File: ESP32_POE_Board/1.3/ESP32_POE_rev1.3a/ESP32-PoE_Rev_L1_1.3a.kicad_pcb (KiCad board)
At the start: 4 copper layers, 28 x 80 mm, 161 parts, among them J1 RS1-02-G, J10 HMTSW-102-X-X-S-X, J11 HMTSW-102-X-X-S-X, J12 HMTSW-102-X-X-S-X, J13 RS1-02-G, J14 RS1-02-G, J15 RS1-02-G, J16 RS1-02-G, J17 RS1-02-G, J18 RS1-02-G, J19 RS1-02-G, J2 HMTSW-102-X-X-S-X, J20 HMTSW-102-X-X-S-X, J21 HMTSW-102-X-X-S-X, J22 HMTSW-102-X-X-S-X, J23 HMTSW-102-X-X-S-X, J24 HMTSW-102-X-X-S-X, J25 SI-46020-F, J26 USB_C_Receptacle, J3 RS1-02-G, J4 RS1-02-G, J5 RS1-02-G, J6 RS1-02-G, J7 HMTSW-102-X-X-S-X, J8 HMTSW-102-X-X-S-X, J9 HMTSW-102-X-X-S-X, Q1 Q12MHz/20pF/10ppm/4P/3.2x2.5mm, Q2 BC817-40(SOT23), Q3 BC817-40(SOT23), SW1 PTS815 SJM 250 SMTR LFS, SW2 PTS815 SJM 250 SMTR LFS, T1 LMUN2211LT1G(SOT-23), U1 CH340T(SSOP20W), U2 TPS2375D(SO-8), U3 BL4054B-42TPRN(SOT23-5), U4 LAN8710A-EZC(QFN32), U5 TX4138(ESOIC-8), U6 ESP32-WROVER-E, U7 SY8089AAAC(SOT23-5), U8 SN74LVC1G04DBVR(SOT23-5)

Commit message: updates
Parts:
- removed ACT1, CHRG1: LED/YELLOW/0603, OLIMEX_LEDs-FP:LED_0603_KA
- removed BAT1: DW02S, OLIMEX_Connectors-FP:LIPO_BAT_VERTICAL_DW02S
- removed BAT_SENS_E1: Opened, OLIMEX_Jumpers-FP:SJ_1_SMALLER
- removed C1, C10, C13, C6, C9: 22uF/6.3V/20%/X5R/C0603, OLIMEX_RLC-FP:C_0603_5MIL_DWS
- removed C11, C14, C15, C16, C18: 100nF/16V/10%/X7R/C0402, OLIMEX_RLC-FP:C_0402_5MIL_DWS
- removed C12, C24: 100nF/100V/10%/X7R/C0603, OLIMEX_RLC-FP:C_0603_5MIL_DWS
- removed C17: 2.2uF/6.3V/10%/X5R/C0603, OLIMEX_RLC-FP:C_0603_5MIL_DWS
- removed C19: 1nF/50V/10%/X7R/C0402, OLIMEX_RLC-FP:C_0402_5MIL_DWS
- removed C2: 1nF/2000V/10%/X7R/C1206, OLIMEX_RLC-FP:C_1206_5MIL_DWS_ISO
- removed C21: NA(10uF/6.3V/20%/X5R/C0603), OLIMEX_RLC-FP:C_0603_5MIL_DWS
- removed C22: 47uF/6.3V/20%/X5R/C0805, OLIMEX_RLC-FP:C_0805_5MIL_DWS
- removed C23: 12pF/50V/5%/COG/C0402, OLIMEX_RLC-FP:C_0402_5MIL_DWS
- removed C25: 470uF/10V/20%/Low_ESR/RM2.5/6.0x11mm, OLIMEX_RLC-FP:CPOL-RM2.5mm_6.3x11mm_PTH
- removed C26: NA(220pF/100V/C0603), OLIMEX_RLC-FP:C_0603_5MIL_DWS
- removed C27: 15uF/100V/20%/RM2.5/6.3x11mm(Farnell:1281844), OLIMEX_RLC-FP:CPOL-RM2.5mm_6.3x11mm_PTH
- removed D1, D3: 1N5822/SS34/SMA, OLIMEX_Diodes-FP:SMA-KA
- removed D5: SS510/100V/5A/0.85V/DO214AB(SMC), OLIMEX_Diodes-FP:DO214AB(SMC)_1(K)-2(A)
- removed D8: SMAJ58A/SMA, OLIMEX_Diodes-FP:SMA-KA
- removed FET1, FET2, FET3: WPM2015-3/TR, OLIMEX_Transistors-FP:SOT23
- removed J1, J13, J14, J15, J16, J17, J18, J19, J3, J4, J5, J6: RS1-02-G, RS1-02-G:CONN_RS1-02-G_ADM
- removed J25: SI-46020-F, SI-46020-F:BEL_SI-46020-F
- removed L1: FB0805/600R/2A, OLIMEX_RLC-FP:L_0805_5MIL_DWS
- removed L2: 2.2uH/1.5A/DCR=72mR/20%/3.00x3.00x1.50mm/CD32(NR3015T2R2M), OLIMEX_RLC-FP:CD32
- removed L4: 33uH/2.1A/DCR=0.1R/20%/DBS135(PD3316MT330), OLIMEX_RLC-FP:DBS135
- removed LAN_CON1: RJP-003TC1(LPJ4112CNL), OLIMEX_Connectors-FP:RJP-003TC1(LPJ4112CNL)
- removed LNK1: LED/GREEN/0603, OLIMEX_LEDs-FP:LED_0603_KA
- removed Logo_OSHW: , OLIMEX_LOGOs-FP:LOGO_OPENHARDWARE_8x8
- removed Logo_Olimex: , OLIMEX_LOGOs-FP:OLIMEX_LOGO_TB
- removed PWR1: LED/RED/0603, OLIMEX_LEDs-FP:LED_0603_KA
- removed R1, R2, R25, R6: 10k/R0402, OLIMEX_RLC-FP:R_0402_5MIL_DWS
- removed R10, R11, R12, R13: 49.9R/1%/R0402, OLIMEX_RLC-FP:R_0402_5MIL_DWS
- removed R14, R15, R41, R5, R8: 2.2k/R0402, OLIMEX_RLC-FP:R_0402_5MIL_DWS
- removed R17, R22: 470k/R0402, OLIMEX_RLC-FP:R_0402_5MIL_DWS
- removed R23: 180k/1%/R0402, OLIMEX_RLC-FP:R_0402_5MIL_DWS
- removed R26: 12.1k/1%/R0402, OLIMEX_RLC-FP:R_0402_5MIL_DWS
- removed R27: 4.42k/1%/1/16W/R0402, OLIMEX_RLC-FP:R_0402_5MIL_DWS
- removed R28: 0.03R/1%/R1206, OLIMEX_RLC-FP:R_1206_5MIL_DWS
- removed R29: 220k/R0402, OLIMEX_RLC-FP:R_0402_5MIL_DWS
- removed R3: 1k/R0402, OLIMEX_RLC-FP:R_0402_5MIL_DWS
- removed R30: 49.9k/1%/R0402, OLIMEX_RLC-FP:R_0402_5MIL_DWS
- removed R33: 4.7R/R0402, OLIMEX_RLC-FP:R_0402_5MIL_DWS
- removed R34: 5.23k/1%/R0402, OLIMEX_RLC-FP:R_0402_5MIL_DWS
- removed R38: 30.1k/1%/R0402, OLIMEX_RLC-FP:R_0402_5MIL_DWS
- removed R4: 47k/R0402, OLIMEX_RLC-FP:R_0402_5MIL_DWS
- removed R42: 4.7k/R2512, OLIMEX_RLC-FP:R_2512_MM_DWS
- removed R43: NA(22R/R0603), OLIMEX_RLC-FP:R_0603_5MIL_DWS
- removed R50: NA(130k/R0402), OLIMEX_RLC-FP:R_0402_5MIL_DWS
- removed R51: NA(10k/R0402), OLIMEX_RLC-FP:R_0402_5MIL_DWS
- removed R7: 24.9k/1%/R0402, OLIMEX_RLC-FP:R_0402_5MIL_DWS
- removed R9: 100k/R0402, OLIMEX_RLC-FP:R_0402_5MIL_DWS
- removed RM1, RM2: RA1206_(4X0603)_4B8_2.2k, OLIMEX_RLC-FP:R_MATRIX_4
- removed Sign_Antistatic: Val**, OLIMEX_LOGOs-FP:LOGO_ANTISTATIC_1
- removed Sign_PB-Free: , OLIMEX_LOGOs-FP:LOGO_PBFREE
- removed Sign_RecycleBin: , OLIMEX_LOGOs-FP:LOGO_RECYCLEBIN_1
- removed T1: LMUN2211LT1G(SOT-23), OLIMEX_Transistors-FP:SOT23
- removed TVS1: ESDS314DBVR(SOT-23-5), OLIMEX_Diodes-FP:SOT-23-5
- removed TVS2, TVS3: NA(GG0402052R542P), OLIMEX_Diodes-FP:D_0402_5MIL_DWS
- removed U2: TPS2375D(SO-8), OLIMEX_IC-FP:SOIC-8_1.75mm
- removed U3: BL4054B-42TPRN(SOT23-5), OLIMEX_IC-FP:SOT-23-5
- removed U4: LAN8710A-EZC(QFN32), OLIMEX_IC-FP:QFN32_EP(33)_5.00x5.00x0.90mm_Pitch_0.50mm
- removed U5: TX4138(ESOIC-8), OLIMEX_Regulators-FP:ESOIC-8
- removed U7: SY8089AAAC(SOT23-5), OLIMEX_Regulators-FP:SOT-23-5
- removed USB-UART1: MISB-SWMM-5B-LF(USB_MICRO), OLIMEX_Connectors-FP:USB-MICRO_MISB-SWMM-5B_LF
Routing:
- net (no net): track 0.00 -> 570.8 mm, vias 0 -> 26
- net +5V: track 91.6 -> 0.00 mm, vias 4 -> 0
- net Spare1: track 84.1 -> 0.00 mm, vias 2 -> 0
- net Spare2: track 83.3 -> 0.00 mm, vias 4 -> 0
- net Net-(C2-Pad2): track 70.5 -> 0.00 mm, vias 13 -> 0
- net GND: track 380.7 -> 330.0 mm, vias 58 -> 55
- net Net-(C11-Pad1): track 46.7 -> 0.00 mm, vias 3 -> 0
- net Net-(U2-PG): track 32.6 -> 0.00 mm, vias 1 -> 0
- net Net-(D5-K): track 30.7 -> 0.00 mm, vias 1 -> 0
- net Net-(R28-Pad1): track 30.0 -> 0.00 mm, vias 7 -> 0
- net Net-(L3-Pad1): track 27.5 -> 0.00 mm
- net Net-(U3-VBAT): track 27.4 -> 0.00 mm, vias 1 -> 0
- net /TD+: track 25.5 -> 0.00 mm, vias 2 -> 0
- net /TD-: track 25.0 -> 0.00 mm, vias 2 -> 0
- net Net-(C10-Pad2): track 24.7 -> 0.00 mm
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- added copper zone on B.Cu, net (none)
- added copper zone on F.Cu, net (none)
- added copper zone on In1.Cu, net (none)
- removed copper zone on B.Cu, net Net-(C2-Pad2)
- removed copper zone on F.Cu, net Net-(C2-Pad2)
- removed copper zone on In1.Cu, net Net-(C2-Pad2)
- removed copper zone on In2.Cu, net Net-(C2-Pad2)
- removed copper zone on F.Cu, net Net-(D5-K)
- removed copper zone on B.Cu, net Net-(R28-Pad1)
- removed copper zone on In1.Cu, net Net-(R28-Pad1)
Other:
- board text removed: "GPIO13"
- board text removed: "GPIO14"

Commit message: board edges
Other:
- board size 28 x 80 mm -> 85 x 80.7 mm
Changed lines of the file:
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@@
   (gr_line (start 90.15 90.15) (end 118.15 90.15)
     (stroke (width 0.254) (type solid)) (layer "Edge.Cuts"))
+  (gr_circle (center 155.1584 150.8252) (end 175.1584 150.8252)
+    (stroke (width 0.05) (type default)) (fill none) (layer "Edge.Cuts"))
   (gr_line (start 90.15 163.83) (end 90.15 170.15)
     (stroke (width 0.254) (type solid)) (layer "Edge.Cuts"))

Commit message: POE1 board
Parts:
- removed H3, H4: MountingHole, MountingHole:MountingHole_2.1mm
- L3, MICRO_SD1, U1: moved to F.Cu
- U6: moved to B.Cu
- moved SW1 94.4 mm to (83.0, 144.7), turned to 180 degrees
- moved SW2 90.6 mm to (84.0, 138.2), turned to 90 degrees
- moved J26 90.6 mm to (92.6, 147.6)
- moved H2 86.3 mm to (79.7, 120.9)
- moved J21 84.6 mm to (76.8, 126.2), turned to 90 degrees
- moved J24 84.4 mm to (76.8, 137.4), turned to 90 degrees
- moved J23 84.1 mm to (76.8, 131.8), turned to 90 degrees
- moved J22 81.2 mm to (79.8, 128.2), turned to 90 degrees
- moved J20 73.7 mm to (79.8, 133.8), turned to 90 degrees
- moved J2 72.9 mm to (79.8, 139.3), turned to 90 degrees
- moved H1 70.8 mm to (105.0, 143.6)
- moved UEXT1 69.1 mm to (165.7, 155.7)
- moved D9 61.7 mm to (155.8, 140.6)
- moved C8 57.5 mm to (153.3, 153.8)
- moved R18 57.5 mm to (149.0, 155.1)
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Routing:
- net (no net): track 570.8 -> 0.00 mm, vias 26 -> 0
- net GND: track 330.0 -> 0.00 mm, vias 55 -> 0
- net /GPI35: track 139.7 -> 0.00 mm, vias 5 -> 0
- net +3.3V: track 100.8 -> 0.00 mm, vias 12 -> 0
- net /GPIO1\U0TXD: track 99.3 -> 0.00 mm, vias 3 -> 0
- net /GPIO16\I2C-SCL: track 95.9 -> 0.00 mm, vias 4 -> 0
- net /GPIO3\U0RXD: track 95.6 -> 0.00 mm, vias 4 -> 0
- net +3.3VLAN: track 90.4 -> 0.00 mm, vias 4 -> 0
- net /GPIO14\HS2_CLK: track 81.1 -> 0.00 mm, vias 2 -> 0
- net /GPIO2\HS2_DATA0: track 78.9 -> 0.00 mm, vias 3 -> 0
- net /GPIO19\EMAC_TXD0(RMII): track 75.2 -> 0.00 mm, vias 3 -> 0
- net /GPIO17\EMAC_CLK_OUT_180: track 74.9 -> 0.00 mm, vias 3 -> 0
- net /GPIO22\EMAC_TXD1(RMII): track 74.7 -> 0.00 mm, vias 2 -> 0
- net /GPIO23\MDC(RMII): track 74.3 -> 0.00 mm, vias 2 -> 0
- net /GPIO21\EMAC_TX_EN(RMII): track 74.3 -> 0.00 mm, vias 3 -> 0
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- removed copper zone on B.Cu, net (none)
- removed copper zone on F.Cu, net (none)
- removed copper zone on In1.Cu, net (none)
- removed copper zone on In2.Cu, net +3.3V
- removed copper zone on B.Cu, net GND
- removed copper zone on F.Cu, net GND
- removed copper zone on In1.Cu, net GND
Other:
- board size 85 x 80.7 mm -> 40 x 40 mm
- board text removed: "(C) 2022"
- board text removed: "+"
- board text removed: "+3V3"
- board text removed: "+5V"
- board text removed: "-"
- board text removed: "1"
- board text removed: "2"
- board text removed: "3"
- board text removed: "4"
- board text removed: "Compliant"
- board text removed: "ESP32-PoE"
- board text removed: "ESP_EN"
- board text removed: "GND"
- board text removed: "GPI34"
- board text removed: "GPI35"
- board text removed: "GPI36"
- board text removed: "GPI39"
- board text removed: "GPIO0"
- board text removed: "GPIO1"
- board text removed: "GPIO15"
- board text removed: "GPIO16"
- board text removed: "GPIO2"
- board text removed: "GPIO3"
- board text removed: "GPIO32"
- board text removed: "GPIO33"
- board text removed: "GPIO4"
- board text removed: "GPIO5"
- board text removed: "Rev.L"
- board text removed: "RoHS"
- board text removed: "www.olimex.com"

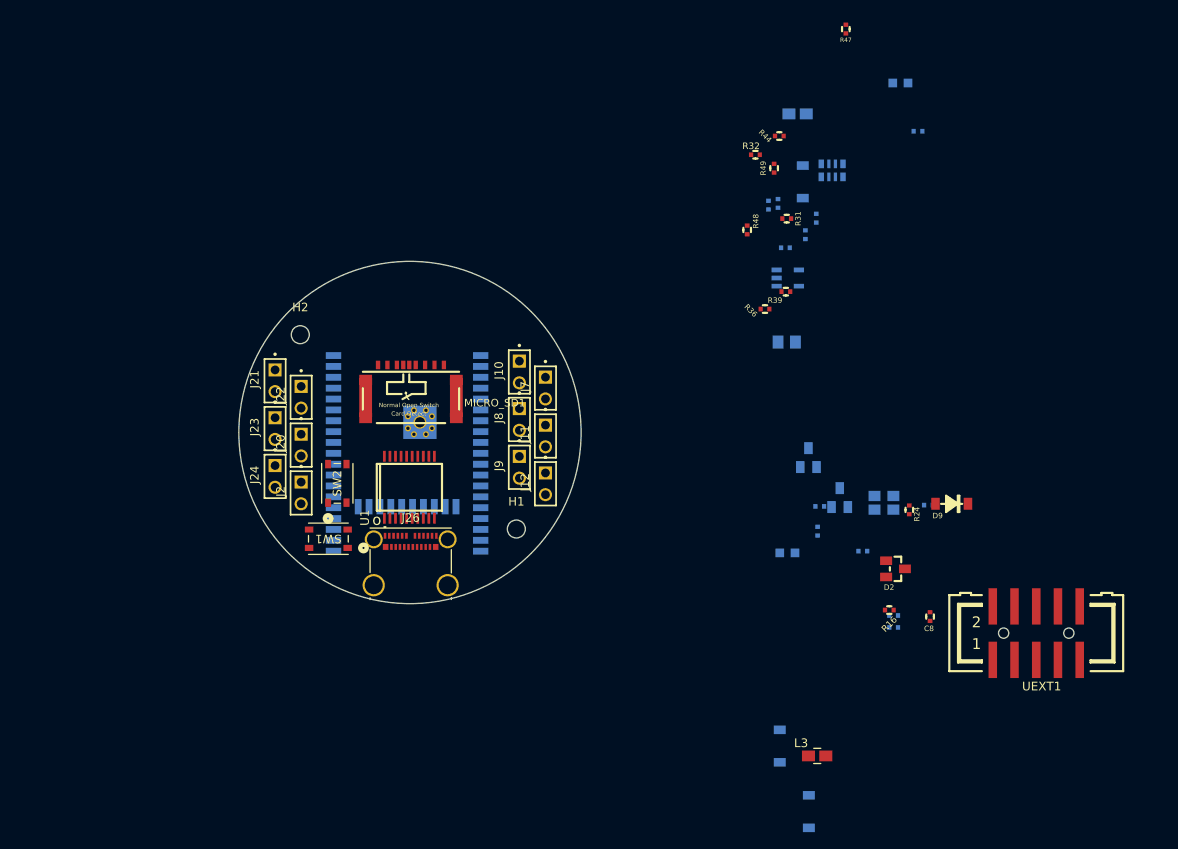
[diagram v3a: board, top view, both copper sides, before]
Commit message: updated power
finished swapping power board bulk cap, new POE board schematic
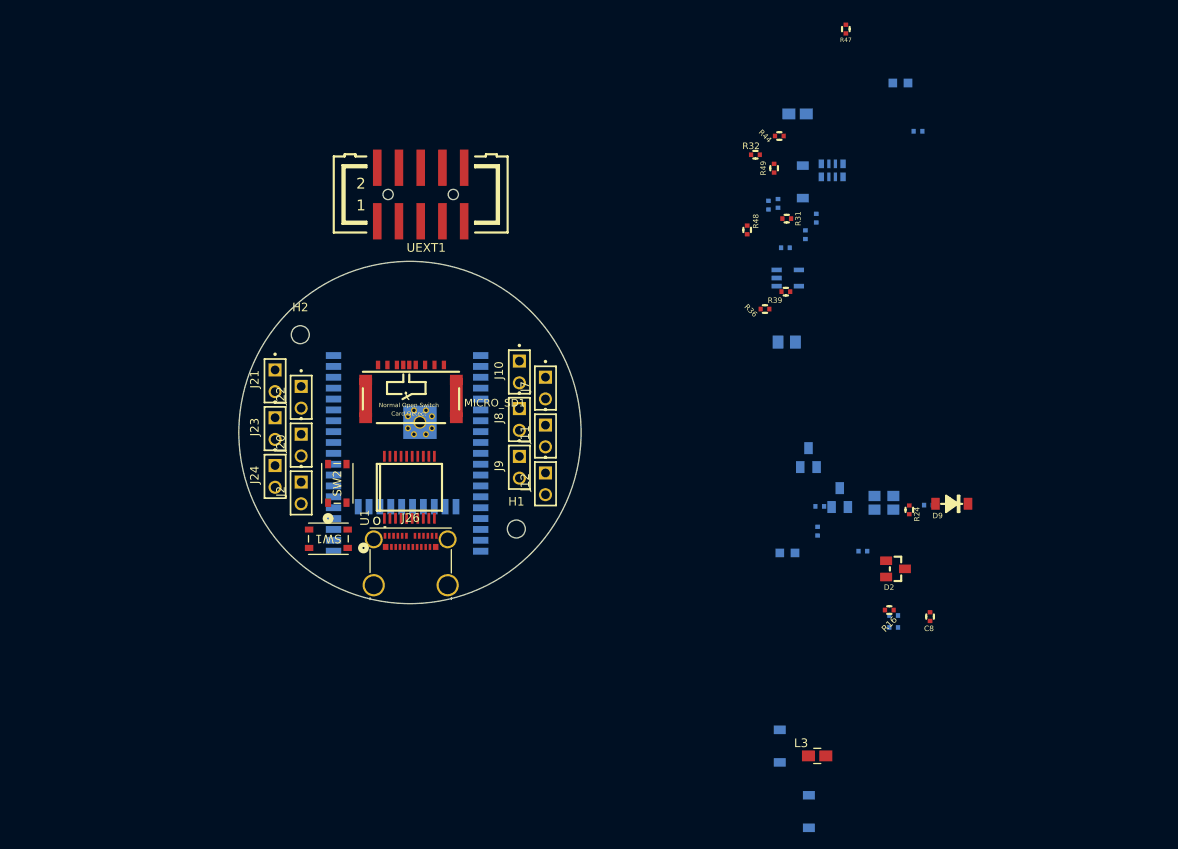
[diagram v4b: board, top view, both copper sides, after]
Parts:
- moved UEXT1 88.3 mm to (93.8, 104.5)
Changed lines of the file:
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@@
   (net 85 "unconnected-(U8-NC-Pad1)")
   (footprint "OLIMEX_Connectors-FP:GBH-254-SMT-10" (layer "F.Cu")
-    (at 165.7096 155.7282)
+    (at 93.7768 104.4694)
     (property "Fieldname 1" "Value 1")
     (property "Fieldname2" "Value2")
@@
     (fp_arc (start 4.09852 -3.14616) (mid 4.664276 -2.911816) (end 4.89862 -2.34606)
       (stroke (width 0.127) (type solid)) (layer "F.Fab"))
-    (fp_arc (start 5.01546 2.071) (mid 4.929028 1.941645) (end 4.898677 1.78906)
-      (stroke (width 0.127) (type solid)) (layer "F.Fab"))
-    (fp_arc (start 5.49806 4.95136) (mid 5.556847 4.809505) (end 5.69872 4.7507)
-      (stroke (width 0.127) (type solid)) (layer "F.Fab"))
-    (fp_arc (start 5.6149 6.06896) (mid 5.5277 5.938437) (end 5.497065 5.78448)
+    (fp_arc (start 5.01546 2.071) (mid 4.929041 1.941642) (end 4.898677 1.78906)
+      (stroke (width 0.127) (type solid)) (layer "F.Fab"))
+    (fp_arc (start 5.49806 4.95136) (mid 5.556855 4.809495) (end 5.69872 4.7507)
+      (stroke (width 0.127) (type solid)) (layer "F.Fab"))
+    (fp_arc (start 5.6149 6.06896) (mid 5.527688 5.938437) (end 5.497065 5.78448)
       (stroke (width 0.127) (type solid)) (layer "F.Fab"))
     (fp_arc (start 6.08226 3.13272) (mid 6.169341 3.262915) (end 6.200095 3.416498)
       (stroke (width 0.127) (type solid)) (layer "F.Fab"))
-    (fp_arc (start 6.1991 4.65164) (mid 6.169328 4.723456) (end 6.0975 4.75324)
+    (fp_arc (start 6.1991 4.65164) (mid 6.169334 4.723492) (end 6.0975 4.75324)
       (stroke (width 0.127) (type solid)) (layer "F.Fab"))
     (fp_arc (start 6.1991 11.0499) (mid 5.964756 11.615656) (end 5.399 11.85)
